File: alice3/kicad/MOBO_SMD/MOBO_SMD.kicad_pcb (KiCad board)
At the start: 2 copper layers, 90.2 x 48.3 mm, 67 parts, among them CON1 MicroSD, J1 VGA, P1 CONN_01X05, P2 USB_OTG, P3 UART1, SW1 RESET, SW2 SOFT RESET, U1 Z80CPU-SMD, U2 Propeller_P8X32A-Q44, U3 24LC256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

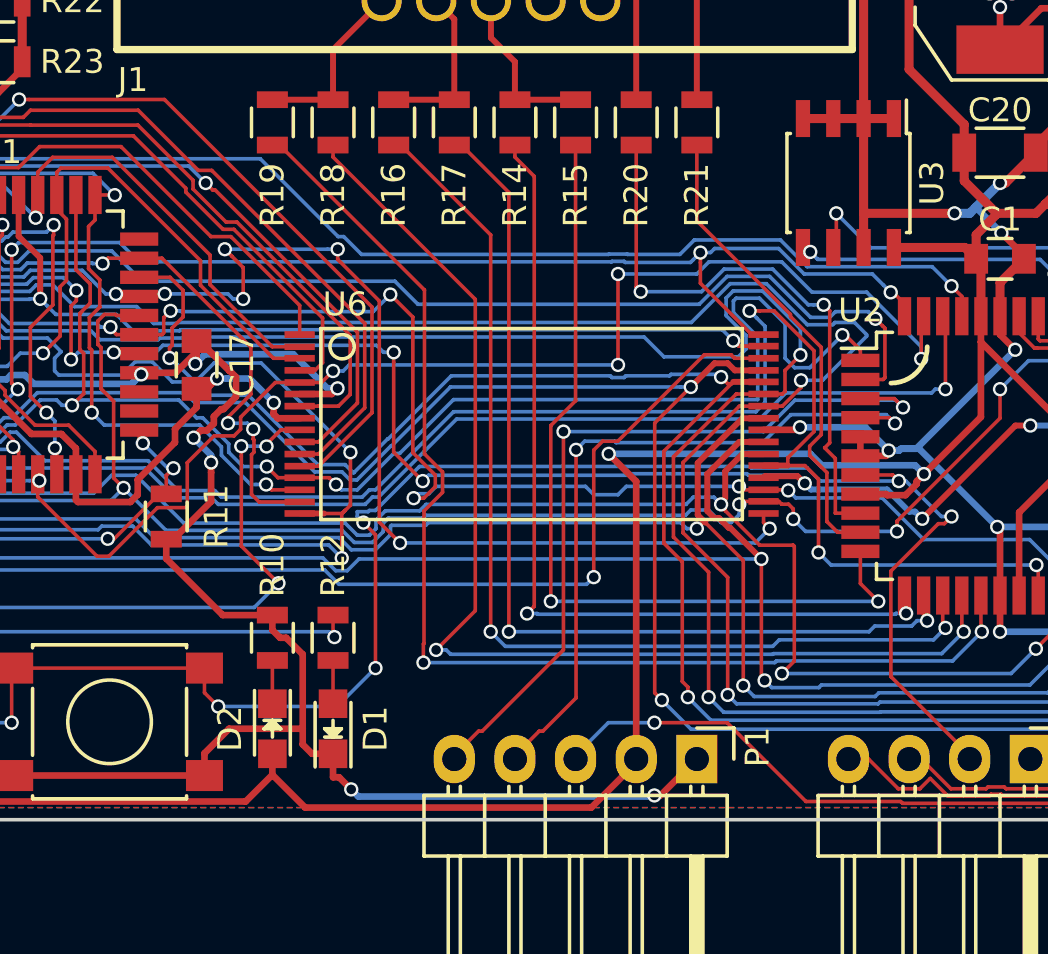
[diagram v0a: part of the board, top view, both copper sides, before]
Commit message: Better 3.3v lines.
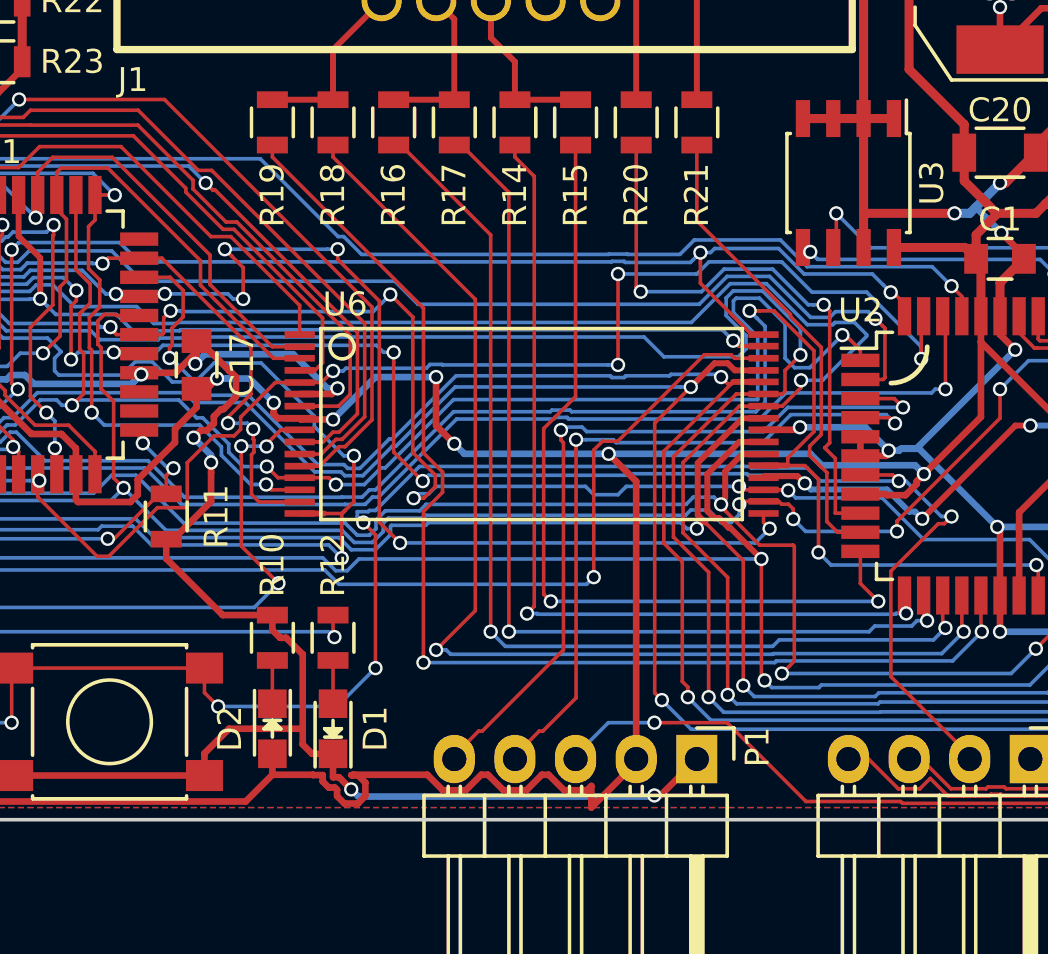
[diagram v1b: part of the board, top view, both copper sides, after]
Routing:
- net +3V3: track 318.9 -> 339.7 mm, vias 4 -> 7

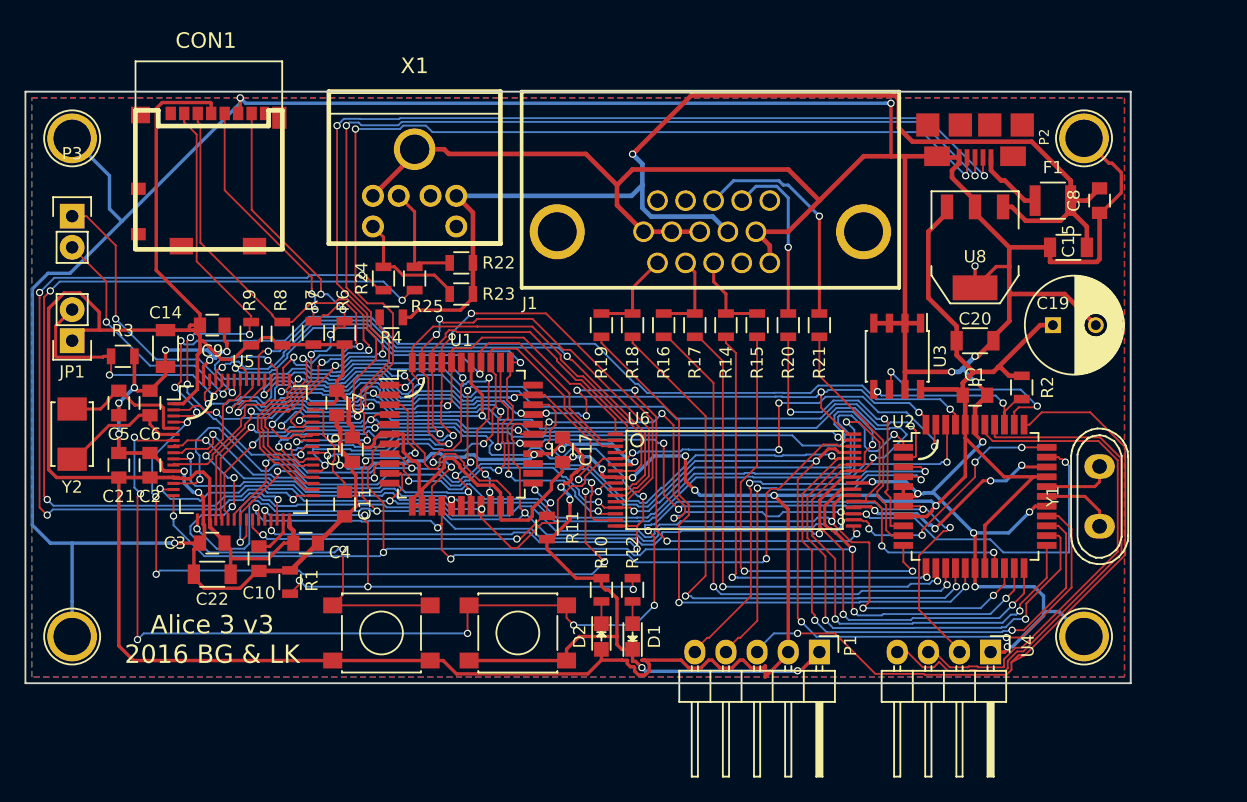
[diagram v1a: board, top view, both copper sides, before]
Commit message: Fix vias on pads.
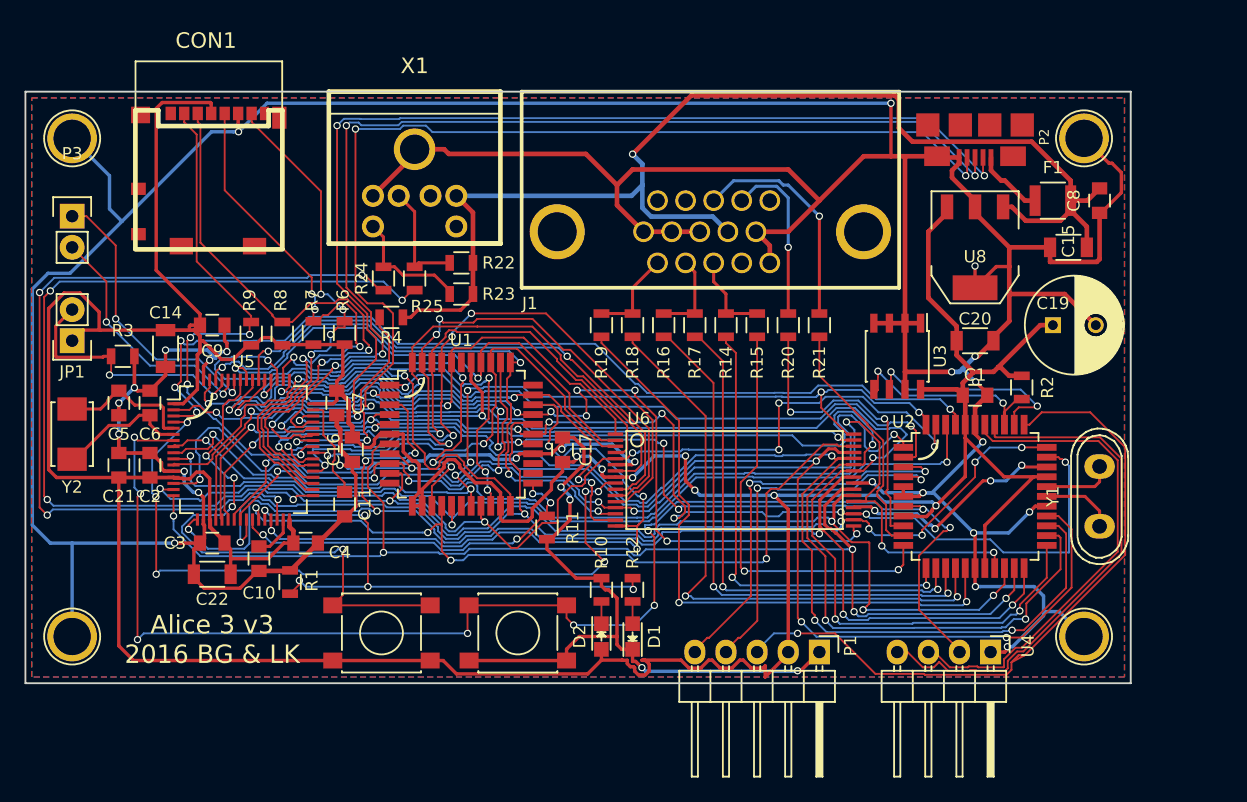
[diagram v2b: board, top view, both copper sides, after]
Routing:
- net /IORQ: track 72.3 -> 75.9 mm
- net D3: track 104.6 -> 106.8 mm
- net Net-(R2-Pad2): track 14.7 -> 16.9 mm
- net A2: track 88.6 -> 90.4 mm
- net D1: track 90.4 -> 92.1 mm
- net /WR: track 80.5 -> 82.2 mm
- net VGA_B0: track 35.9 -> 34.6 mm
- net Net-(SW2-Pad1): track 43.8 -> 45.1 mm
- net A4: track 53.3 -> 54.5 mm
- net /Z80_RESET: track 29.4 -> 30.4 mm
- net VGA_R0: track 50.4 -> 51.4 mm
- net VGA_B1: track 36.8 -> 37.6 mm
- net VGA_G0: track 40.4 -> 41.1 mm
- net VGA_R1: track 48.4 -> 49.2 mm
- net VGA_G1: track 43.3 -> 43.9 mm

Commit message: V4 improvements round 2
Label buttons, LEDs, and connectors

Delete footprints for deleted schematic parts

Move microUSB jack and space out PS2, VGA connectors

Position SMT Propeller crystal

Change BOOT0 header to button

Delete RAM
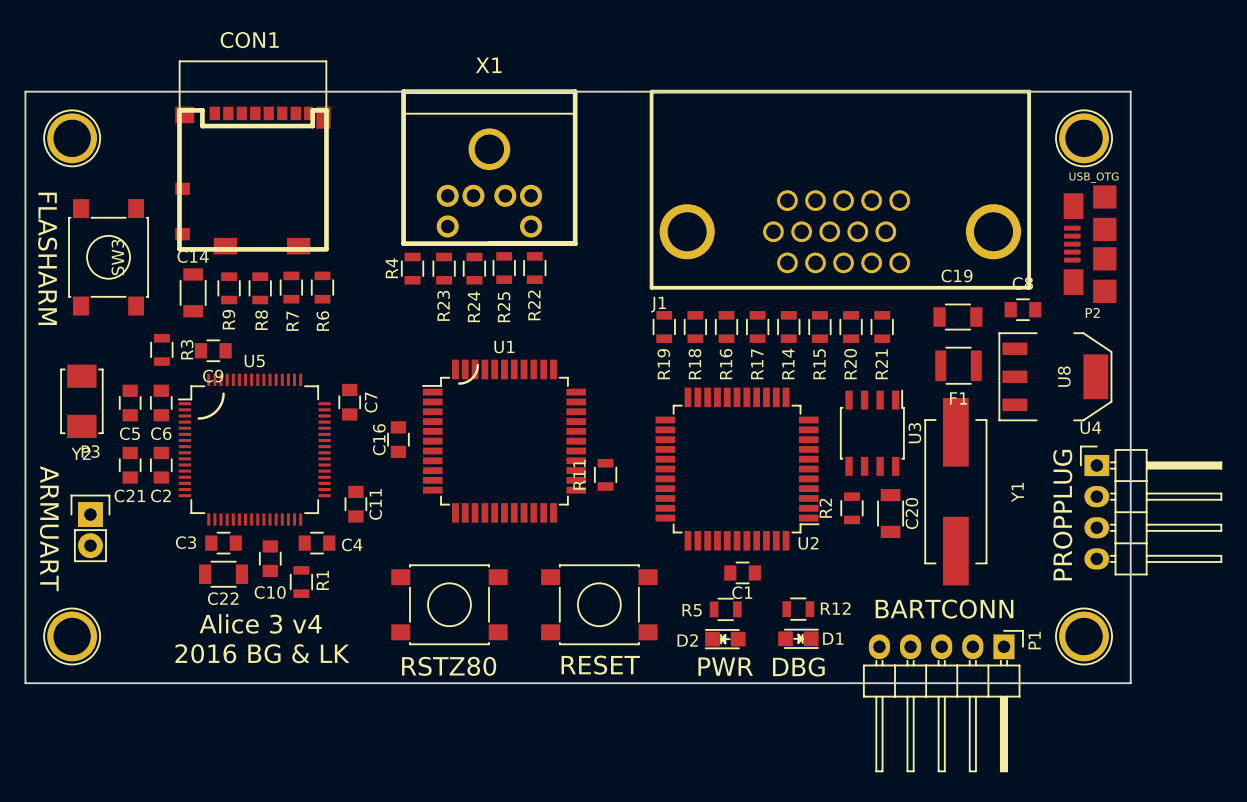
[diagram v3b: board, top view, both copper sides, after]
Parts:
- removed C15: 1000 µF, Capacitors_ThroughHole:C_Radial_D8_L11.5_P3.5
- removed C17: 0.1 µF, Capacitors_SMD:C_0805
- removed JP1: Jumper_NO_Small, Pin_Headers:Pin_Header_Straight_1x02
- removed R10: 100, Resistors_SMD:R_0805
- removed U6: AS6C2008_TSOP, SMD_Packages:TSOP32SP
- added R5: 100, Resistors_SMD:R_0805, F.Cu at (166.3, 115.9)
- added SW3: FLASH ARM, Buttons_Switches_SMD:SW_SPST_PTS645, F.Cu at (116.0, 87.2)
- Y1: footprint Crystals:Crystal_HC50-U_Vertical -> Crystals:Crystal_HC49-SD_SMD
- moved P3 24.4 mm to (114.5, 108.2)
- moved C1 23.9 mm to (167.7, 112.9), turned to 180 degrees
- moved U2 19.5 mm to (167.3, 104.5), turned to 180 degrees
- moved U4 17.5 mm to (196.6, 104.2), turned to 0 degrees
- moved R2 17.0 mm to (176.7, 107.7), turned to 90 degrees
- moved P2 16.4 mm to (198.7, 86.1), turned to 90 degrees
- moved C20 15.7 mm to (179.8, 108.1), turned to 270 degrees
- moved F1 15.5 mm to (185.3, 96.0), turned to 180 degrees
- moved P1 15.1 mm to (189.1, 119.0)
- moved R12 13.6 mm to (172.3, 115.9), turned to 180 degrees
- moved D1 13.5 mm to (172.3, 118.3), turned to 180 degrees
- moved U8 12.4 mm to (193.2, 96.9), turned to 270 degrees
- moved Y1 11.7 mm to (185.1, 106.3), turned to 270 degrees
- moved C8 10.9 mm to (190.6, 91.5), turned to 0 degrees
- moved C19 10.7 mm to (185.3, 92.0), turned to 0 degrees
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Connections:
- net /BUSACK renamed ~BUSACK
- net /BUSRQ renamed ~BUSRQ
- net /HALT renamed ~HALT
- net /IORQ renamed ~IORQ
- net /MREQ renamed ~MREQ
- net /RD renamed ~RD
- net /RESET renamed ~RESET
- net /WR renamed ~WR
- net /Z80_RESET renamed ~Z80_RESET
- P2 pad S4: GND -> (no net)
- U1 pad 21: +3V3 -> ~WAIT
- U1 pad 25: Net-(U1-Pad25) -> ~RFSH
- U5 pad 4: A17 -> ~RFSH
- U5 pad 54: A16 -> ~WAIT
- U8 pad 4: GND -> (no net)
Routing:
- net GND: track 496.1 -> 0.00 mm, vias 30 -> 0
- net +3V3: track 339.8 -> 0.00 mm, vias 7 -> 0
- net ~RESET: track 114.5 -> 0.00 mm, vias 9 -> 0
- net D5: track 112.0 -> 0.00 mm, vias 5 -> 0
- net D4: track 111.6 -> 0.00 mm, vias 5 -> 0
- net D6: track 107.0 -> 0.00 mm, vias 5 -> 0
- net D3: track 106.8 -> 0.00 mm, vias 7 -> 0
- net D7: track 106.7 -> 0.00 mm, vias 5 -> 0
- net +5V: track 100.4 -> 0.00 mm, vias 1 -> 0
- net D2: track 99.0 -> 0.00 mm, vias 5 -> 0
- net D0: track 96.6 -> 0.00 mm, vias 6 -> 0
- net USB_ID: track 92.3 -> 0.00 mm, vias 4 -> 0
- net USB_D_N: track 92.2 -> 0.00 mm, vias 4 -> 0
- net D1: track 92.1 -> 0.00 mm, vias 5 -> 0
- net A2: track 90.4 -> 0.00 mm, vias 7 -> 0
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- removed copper zone on F.Cu, net +3V3
- removed copper zone on B.Cu, net GND
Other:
- board text added: "ARMUART"
- board text added: "Alice 3 v4 2016 BG & LK"
- board text added: "BARTCONN"
- board text added: "DBG"
- board text added: "FLASHARM"
- board text added: "PROPPLUG"
- board text added: "PWR"
- board text added: "RESET"
- board text added: "RSTZ80"
- board text removed: "Alice 3 v3 2016 BG & LK"
